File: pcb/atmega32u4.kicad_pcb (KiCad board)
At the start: 2 copper layers, 15 parts, among them CON1 ISP, P1 CONN_01X14, P2 CONN_01X14, P3 USB_OTG, U1 ATmega32U4-AU, Y1 16MHz

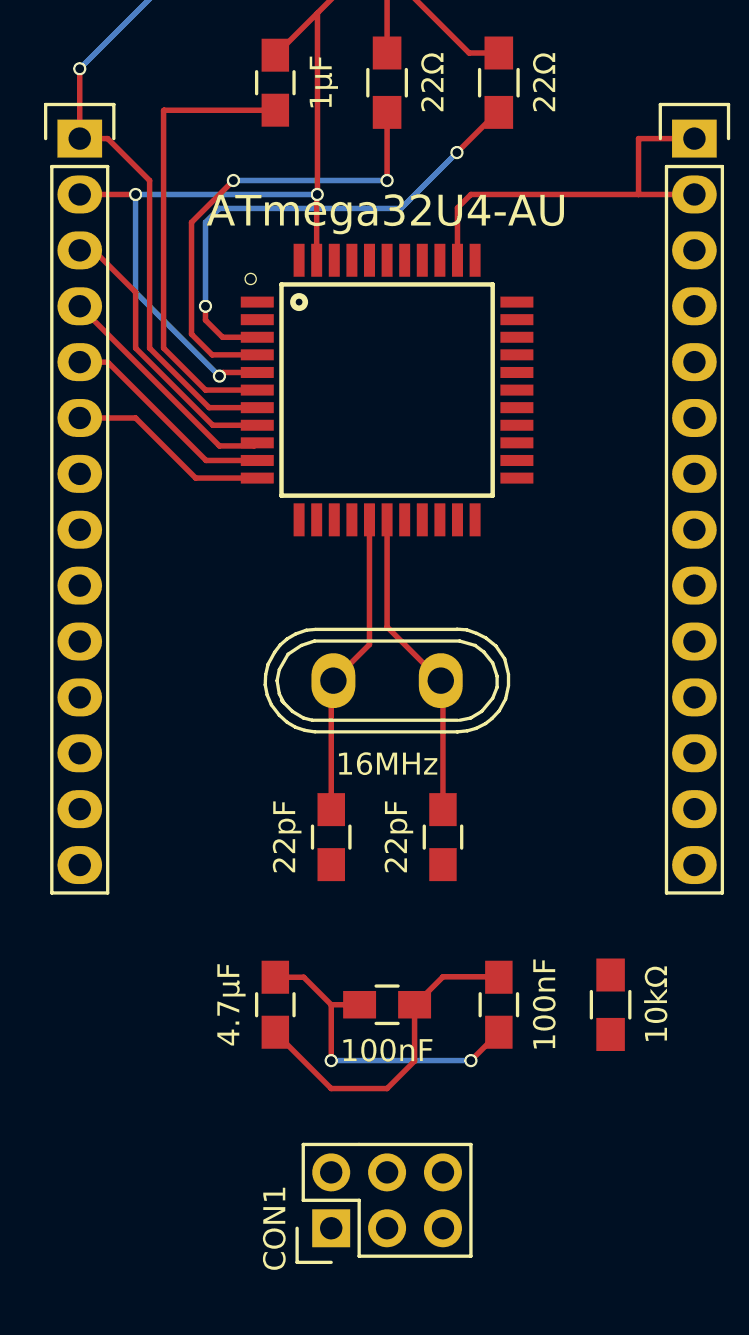
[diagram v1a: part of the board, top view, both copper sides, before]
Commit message: Finish left side and programming header
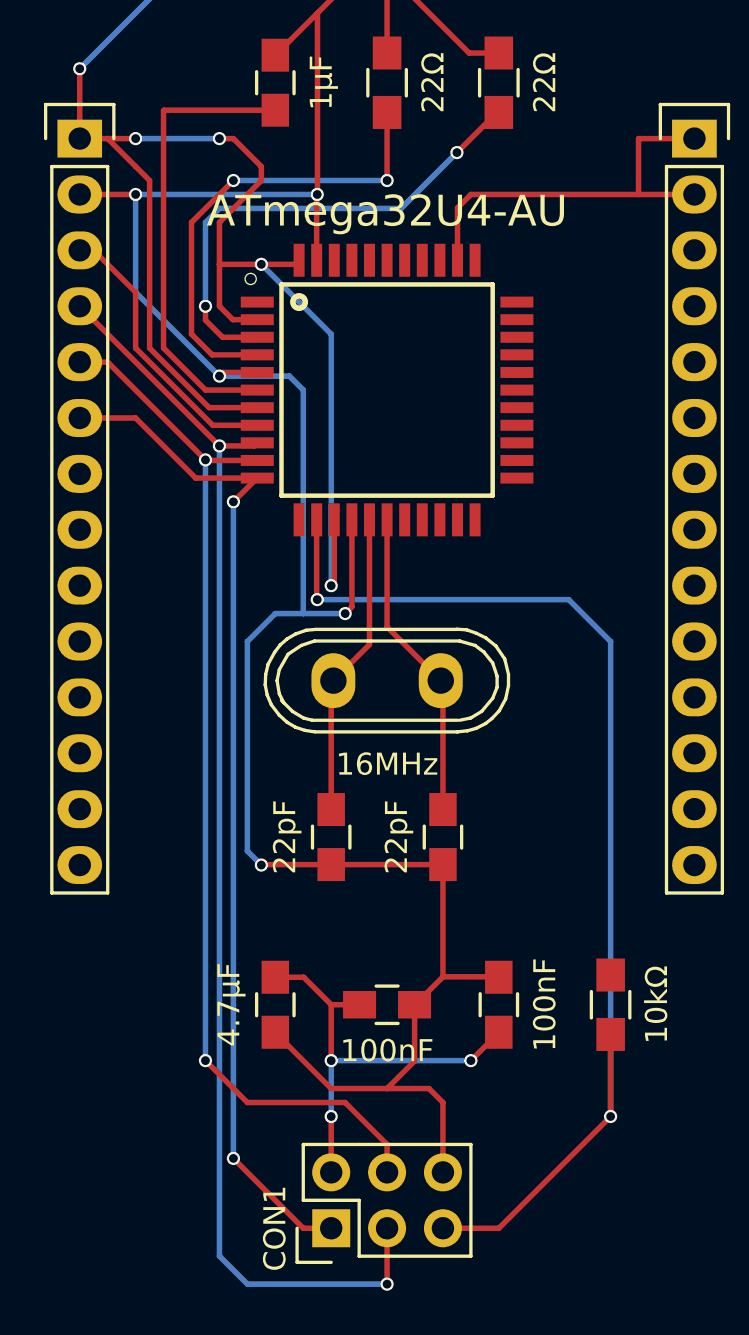
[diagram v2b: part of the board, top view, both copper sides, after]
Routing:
- net GND: track 74.6 -> 128.0 mm, vias 3 -> 5
- net /ISP_RESET: track 0.00 -> 52.8 mm, vias 0 -> 2
- net /ISP_SCK/PB1: track 10.8 -> 58.3 mm, vias 0 -> 2
- net /VCC: track 41.0 -> 80.3 mm, vias 2 -> 6
- net /ISP_MOSI/PB2: track 9.92 -> 48.4 mm, vias 0 -> 2
- net /ISP_MISO/PB3: track 9.20 -> 46.3 mm, vias 0 -> 2
- net +5V: track 15.1 -> 20.1 mm, vias 2 -> 3
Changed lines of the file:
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@@
   (general
     (links 67)
-    (no_connects 42)
+    (no_connects 28)
     (area 119.426667 76.775 157.433334 145.733809)
     (thickness 1.6)
     (drawings 0)
-    (tracks 103)
+    (tracks 178)
     (zones 0)
     (modules 15)
@@
       (net 5 /XTAL2))
   )
+  (segment (start 135.89 135.89) (end 135.89 138.43) (width 0.25) (layer B.Cu) (net 1))
+  (segment (start 135.89 138.43) (end 135.89 140.97) (width 0.25) (layer F.Cu) (net 1))
+  (via (at 135.89 138.43) (size 0.6) (drill 0.4) (layers F.Cu B.Cu) (net 1))
   (segment (start 133.35 132.1) (end 134.64 132.1) (width 0.25) (layer F.Cu) (net 1))
   (segment (start 134.64 132.1) (end 135.89 133.35) (width 0.25) (layer F.Cu) (net 1))
@@
   (segment (start 135.89 135.89) (end 135.89 133.35) (width 0.25) (layer F.Cu) (net 1))
   (segment (start 135.89 133.35) (end 137.18 133.35) (width 0.25) (layer F.Cu) (net 1))
+  (segment (start 134.62 115.57) (end 134.62 105.41) (width 0.25) (layer B.Cu) (net 2))
+  (segment (start 133.985 104.775) (end 130.81 104.775) (width 0.25) (layer B.Cu) (net 2))
+  (segment (start 134.62 105.41) (end 133.985 104.775) (width 0.25) (layer B.Cu) (net 2))
+  (segment (start 135.89 126.98) (end 132.735 126.98) (width 0.25) (layer F.Cu) (net 2))
+  (segment (start 136.83 115.265) (end 136.83 111.31) (width 0.25) (layer F.Cu) (net 2))
+  (segment (start 136.525 115.57) (end 136.83 115.265) (width 0.25) (layer F.Cu) (net 2))
+  (via (at 136.525 115.57) (size 0.6) (drill 0.4) (layers F.Cu B.Cu) (net 2))
+  (segment (start 133.35 115.57) (end 134.62 115.57) (width 0.25) (layer B.Cu) (net 2))
+  (segment (start 134.62 115.57) (end 136.525 115.57) (width 0.25) (layer B.Cu) (net 2))
+  (segment (start 132.08 116.84) (end 133.35 115.57) (width 0.25) (layer B.Cu) (net 2))
+  (segment (start 132.08 126.365) (end 132.08 116.84) (width 0.25) (layer B.Cu) (net 2))
+  (segment (start 132.715 127) (end 132.08 126.365) (width 0.25) (layer B.Cu) (net 2))
+  (via (at 132.715 127) (size 0.6) (drill 0.4) (layers F.Cu B.Cu) (net 2))
+  (segment (start 132.735 126.98) (end 132.715 127) (width 0.25) (layer F.Cu) (net 2))
+  (segment (start 140.97 126.98) (end 135.89 126.98) (width 0.25) (layer F.Cu) (net 2))
+  (segment (start 140.97 132.08) (end 140.97 126.98) (width 0.25) (layer F.Cu) (net 2))
+  (segment (start 138.43 137.16) (end 140.335 137.16) (width 0.25) (layer F.Cu) (net 2))
+  (segment (start 140.97 137.795) (end 140.97 140.97) (width 0.25) (layer F.Cu) (net 2))
+  (segment (start 140.335 137.16) (end 140.97 137.795) (width 0.25) (layer F.Cu) (net 2))
   (segment (start 127 100.965) (end 127 96.52) (width 0.25) (layer B.Cu) (net 2))
   (segment (start 130.81 104.775) (end 127 100.965) (width 0.25) (layer B.Cu) (net 2))
   (via (at 130.81 104.775) (size 0.6) (drill 0.4) (layers F.Cu B.Cu) (net 2))
+  (segment (start 132.53 104.61) (end 130.975 104.61) (width 0.25) (layer F.Cu) (net 2))
   (segment (start 130.975 104.61) (end 130.81 104.775) (width 0.25) (layer F.Cu) (net 2))
-  (segment (start 132.53 104.61) (end 130.975 104.61) (width 0.25) (layer F.Cu) (net 2))
   (segment (start 135.265 88.275) (end 135.265 96.51) (width 0.25) (layer F.Cu) (net 2))
   (segment (start 135.265 96.51) (end 135.255 96.52) (width 0.25) (layer F.Cu) (net 2))
@@
   (segment (start 137.63 111.31) (end 137.63 116.97706) (width 0.25) (layer F.Cu) (net 5))
   (segment (start 137.63 116.97706) (end 135.98906 118.618) (width 0.25) (layer F.Cu) (net 5))
+  (via (at 148.59 138.43) (size 0.6) (drill 0.4) (layers F.Cu B.Cu) (net 6))
+  (segment (start 135.23 111.31) (end 135.23 114.91) (width 0.25) (layer F.Cu) (net 6))
+  (segment (start 148.59 116.84) (end 148.59 138.43) (width 0.25) (layer B.Cu) (net 6))
+  (segment (start 146.685 114.935) (end 148.59 116.84) (width 0.25) (layer B.Cu) (net 6))
+  (segment (start 135.255 114.935) (end 146.685 114.935) (width 0.25) (layer B.Cu) (net 6))
+  (via (at 135.255 114.935) (size 0.6) (drill 0.4) (layers F.Cu B.Cu) (net 6))
+  (segment (start 135.23 114.91) (end 135.255 114.935) (width 0.25) (layer F.Cu) (net 6))
+  (segment (start 148.59 134.7) (end 148.59 138.43) (width 0.25) (layer F.Cu) (net 6))
+  (segment (start 143.51 143.51) (end 140.97 143.51) (width 0.25) (layer F.Cu) (net 6))
+  (segment (start 148.59 138.43) (end 143.51 143.51) (width 0.25) (layer F.Cu) (net 6))
   (segment (start 124.46 99.06) (end 125.095 99.06) (width 0.25) (layer F.Cu) (net 7))
   (segment (start 125.095 99.06) (end 127 100.965) (width 0.25) (layer F.Cu) (net 7))
@@
   (segment (start 127 103.503602) (end 130.506398 107.01) (width 0.25) (layer F.Cu) (net 7))
   (segment (start 130.506398 107.01) (end 132.53 107.01) (width 0.25) (layer F.Cu) (net 7))
+  (via (at 130.81 107.95) (size 0.6) (drill 0.4) (layers F.Cu B.Cu) (net 8))
+  (segment (start 138.43 143.51) (end 138.43 146.05) (width 0.25) (layer F.Cu) (net 8))
+  (via (at 138.43 146.05) (size 0.6) (drill 0.4) (layers F.Cu B.Cu) (net 8))
+  (segment (start 132.08 146.05) (end 138.43 146.05) (width 0.25) (layer B.Cu) (net 8))
+  (segment (start 130.81 144.78) (end 132.08 146.05) (width 0.25) (layer B.Cu) (net 8))
+  (segment (start 130.81 144.78) (end 130.81 107.95) (width 0.25) (layer B.Cu) (net 8))
   (segment (start 124.46 101.6) (end 130.81 107.95) (width 0.25) (layer F.Cu) (net 8))
   (segment (start 130.81 107.95) (end 132.39 107.95) (width 0.25) (layer F.Cu) (net 8))
   (segment (start 132.39 107.95) (end 132.53 107.81) (width 0.25) (layer F.Cu) (net 8))
+  (segment (start 130.175 108.585) (end 130.2 108.61) (width 0.25) (layer F.Cu) (net 9))
+  (via (at 130.175 108.585) (size 0.6) (drill 0.4) (layers F.Cu B.Cu) (net 9))
+  (segment (start 130.175 135.89) (end 130.175 108.585) (width 0.25) (layer B.Cu) (net 9))
+  (via (at 130.175 135.89) (size 0.6) (drill 0.4) (layers F.Cu B.Cu) (net 9))
+  (segment (start 132.08 137.795) (end 130.175 135.89) (width 0.25) (layer F.Cu) (net 9))
+  (segment (start 136.525 137.795) (end 132.08 137.795) (width 0.25) (layer F.Cu) (net 9))
+  (segment (start 138.43 139.7) (end 136.525 137.795) (width 0.25) (layer F.Cu) (net 9))
+  (segment (start 138.43 140.97) (end 138.43 139.7) (width 0.25) (layer F.Cu) (net 9))
   (segment (start 124.46 104.14) (end 125.73 104.14) (width 0.25) (layer F.Cu) (net 9))
   (segment (start 130.2 108.61) (end 132.53 108.61) (width 0.25) (layer F.Cu) (net 9))
   (segment (start 125.73 104.14) (end 130.2 108.61) (width 0.25) (layer F.Cu) (net 9))
+  (segment (start 132.53 109.41) (end 132.525 109.41) (width 0.25) (layer F.Cu) (net 10))
+  (segment (start 132.525 109.41) (end 131.445 110.49) (width 0.25) (layer F.Cu) (net 10))
+  (segment (start 134.62 143.51) (end 135.89 143.51) (width 0.25) (layer F.Cu) (net 10))
+  (segment (start 131.445 140.335) (end 134.62 143.51) (width 0.25) (layer F.Cu) (net 10))
+  (via (at 131.445 140.335) (size 0.6) (drill 0.4) (layers F.Cu B.Cu) (net 10))
+  (segment (start 131.445 110.49) (end 131.445 140.335) (width 0.25) (layer B.Cu) (net 10))
+  (via (at 131.445 110.49) (size 0.6) (drill 0.4) (layers F.Cu B.Cu) (net 10))
   (segment (start 124.46 106.68) (end 127 106.68) (width 0.25) (layer F.Cu) (net 10))
   (segment (start 129.73 109.41) (end 132.53 109.41) (width 0.25) (layer F.Cu) (net 10))
@@
   (segment (start 130.95 103.01) (end 130.175 102.235) (width 0.25) (layer F.Cu) (net 36))
   (segment (start 143.43 92.79) (end 143.51 92.79) (width 0.25) (layer F.Cu) (net 36))
+  (segment (start 136.03 111.31) (end 136.03 114.16) (width 0.25) (layer F.Cu) (net 40) (status 400000))
+  (via (at 132.715 99.695) (size 0.6) (drill 0.4) (layers F.Cu B.Cu) (net 40))
+  (segment (start 135.89 102.87) (end 132.715 99.695) (width 0.25) (layer B.Cu) (net 40))
+  (segment (start 135.89 114.3) (end 135.89 102.87) (width 0.25) (layer B.Cu) (net 40))
+  (via (at 135.89 114.3) (size 0.6) (drill 0.4) (layers F.Cu B.Cu) (net 40))
+  (segment (start 136.03 114.16) (end 135.89 114.3) (width 0.25) (layer F.Cu) (net 40))
+  (segment (start 130.81 99.695) (end 132.715 99.695) (width 0.25) (layer F.Cu) (net 40))
+  (segment (start 132.715 99.695) (end 134.245 99.695) (width 0.25) (layer F.Cu) (net 40))
+  (segment (start 134.245 99.695) (end 134.43 99.51) (width 0.25) (layer F.Cu) (net 40))
+  (segment (start 125.73 93.98) (end 127 93.98) (width 0.25) (layer F.Cu) (net 40))
+  (segment (start 131.42 102.21) (end 130.81 101.6) (width 0.25) (layer F.Cu) (net 40))
+  (segment (start 130.81 101.6) (end 130.81 99.695) (width 0.25) (layer F.Cu) (net 40))
+  (segment (start 130.81 99.695) (end 130.81 97.79) (width 0.25) (layer F.Cu) (net 40))
+  (segment (start 130.81 97.79) (end 132.715 95.885) (width 0.25) (layer F.Cu) (net 40))
+  (segment (start 132.715 95.885) (end 132.715 95.25) (width 0.25) (layer F.Cu) (net 40))
+  (segment (start 132.715 95.25) (end 131.445 93.98) (width 0.25) (layer F.Cu) (net 40))
+  (segment (start 131.445 93.98) (end 130.81 93.98) (width 0.25) (layer F.Cu) (net 40))
+  (via (at 130.81 93.98) (size 0.6) (drill 0.4) (layers F.Cu B.Cu) (net 40))
+  (segment (start 130.81 93.98) (end 127 93.98) (width 0.25) (layer B.Cu) (net 40))
+  (via (at 127 93.98) (size 0.6) (drill 0.4) (layers F.Cu B.Cu) (net 40))
+  (segment (start 131.42 102.21) (end 132.53 102.21) (width 0.25) (layer F.Cu) (net 40))
   (segment (start 132.53 106.21) (end 130.342796 106.21) (width 0.25) (layer F.Cu) (net 40))
   (segment (start 125.73 93.98) (end 124.46 93.98) (width 0.25) (layer F.Cu) (net 40))
-  (segment (start 127.635 95.885) (end 125.73 93.98) (width 0.25) (layer F.Cu) (net 40))
+  (segment (start 127.635 95.885) (end 127 95.25) (width 0.25) (layer F.Cu) (net 40))
+  (segment (start 127 95.25) (end 125.73 93.98) (width 0.25) (layer F.Cu) (net 40))
   (segment (start 127.635 103.502204) (end 127.635 95.885) (width 0.25) (layer F.Cu) (net 40))
   (segment (start 130.342796 106.21) (end 127.635 103.502204) (width 0.25) (layer F.Cu) (net 40))

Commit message: Commit before cleanup
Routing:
- net /PF7: track 0.00 -> 44.4 mm, vias 0 -> 2
- net /PF6: track 0.00 -> 40.6 mm, vias 0 -> 2
- net /PD0: track 0.00 -> 33.7 mm, vias 0 -> 2
- net /PC7: track 0.00 -> 33.6 mm, vias 0 -> 4
- net /PF5: track 0.00 -> 33.4 mm, vias 0 -> 2
- net /PF4: track 0.00 -> 31.6 mm, vias 0 -> 2
- net /PC6: track 0.00 -> 30.9 mm, vias 0 -> 4
- net /PB5: track 0.00 -> 29.2 mm, vias 0 -> 2
- net /PD1: track 0.00 -> 29.2 mm, vias 0 -> 2
- net /PB4: track 0.00 -> 27.8 mm, vias 0 -> 2
- net /PD2: track 0.00 -> 24.3 mm, vias 0 -> 2
- net /PB6: track 0.00 -> 24.2 mm, vias 0 -> 2
- net /VCC: track 80.3 -> 60.5 mm, vias 6 -> 5
- net /PD3: track 0.00 -> 19.8 mm, vias 0 -> 2
- net /PD7: track 0.00 -> 16.2 mm, vias 0 -> 2
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
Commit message: jk I didn’t do cleanup. I finished the connections
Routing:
- net /VCC: track 60.5 -> 160.0 mm, vias 5 -> 9
- net /PF1: track 0.00 -> 58.6 mm, vias 0 -> 2
- net /PF0: track 0.00 -> 53.2 mm, vias 0 -> 2
- net GND: track 125.9 -> 164.0 mm, vias 6 -> 10
- net Net-(P3-Pad6): track 0.00 -> 13.7 mm

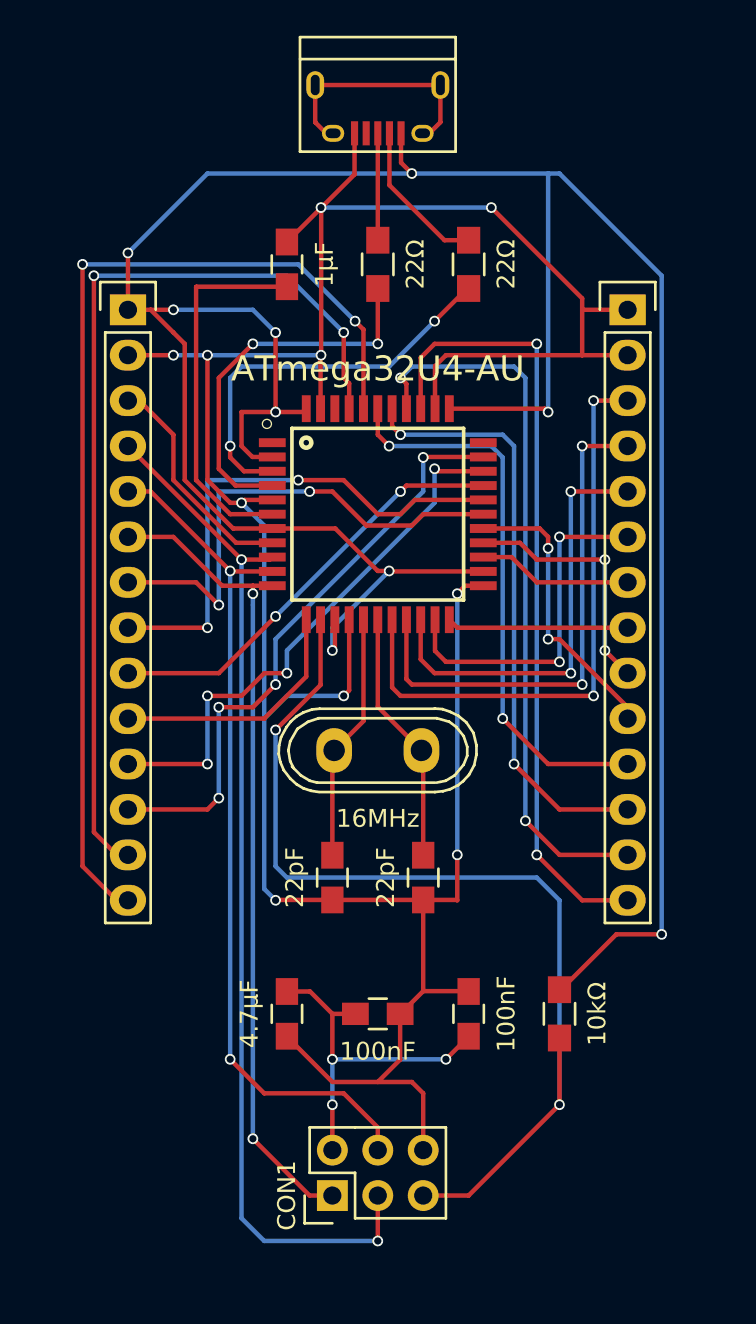
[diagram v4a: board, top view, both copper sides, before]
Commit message: Add outline to board
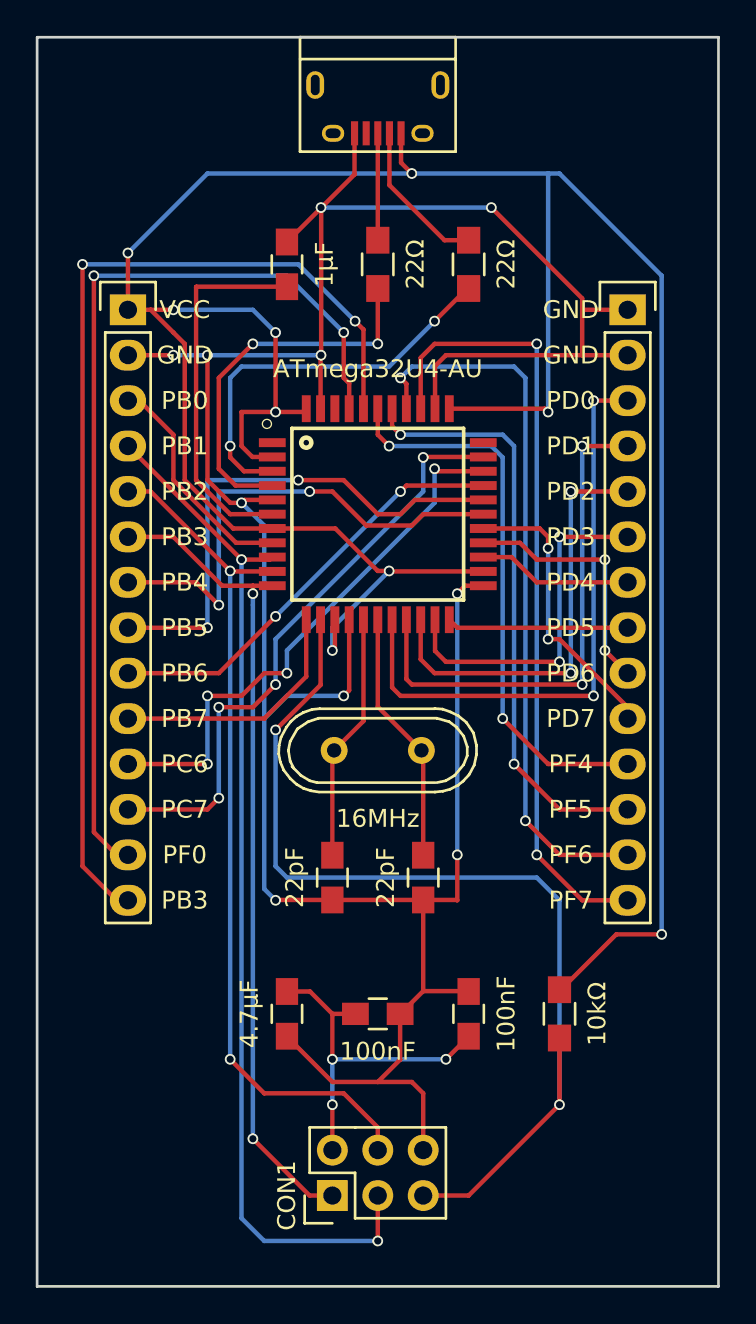
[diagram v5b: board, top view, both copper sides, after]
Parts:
- Y1: footprint Crystals:Crystal_HC50-U_Vertical -> Crystals:Crystal_HC49-U_Vertical
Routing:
- net Net-(P3-Pad6): track 13.7 -> 0.76 mm
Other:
- board outline added: 38.1 x 69.9 mm
- net class Default: clearance 0.2 -> 0.1524; trace_width 0.25 -> 0.1524; via_dia 0.6 -> 0.6858; via_drill 0.4 -> 0.3302
- rule trace_clearance: 0.2 -> 0.1524
- rule trace_min: 0.2 -> 0.1524
- rule via_min_drill: 0.3 -> 0.3302
- rule via_min_size: 0.4 -> 0.6858
- board text added: "GND"
- board text added: "PB0"
- board text added: "PB1"
- board text added: "PB2"
- board text added: "PB3"
- board text added: "PB4"
- board text added: "PB5"
- board text added: "PB6"
- board text added: "PB7"
- board text added: "PC6"
- board text added: "PC7"
- board text added: "PD0"
- board text added: "PD1"
- board text added: "PD2"
- board text added: "PD3"
- board text added: "PD4"
- board text added: "PD5"
- board text added: "PD6"
- board text added: "PD7"
- board text added: "PF0"
- board text added: "PF4"
- board text added: "PF5"
- board text added: "PF6"
- board text added: "PF7"
- board text added: "VCC"
